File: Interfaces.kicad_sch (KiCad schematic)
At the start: 0 parts

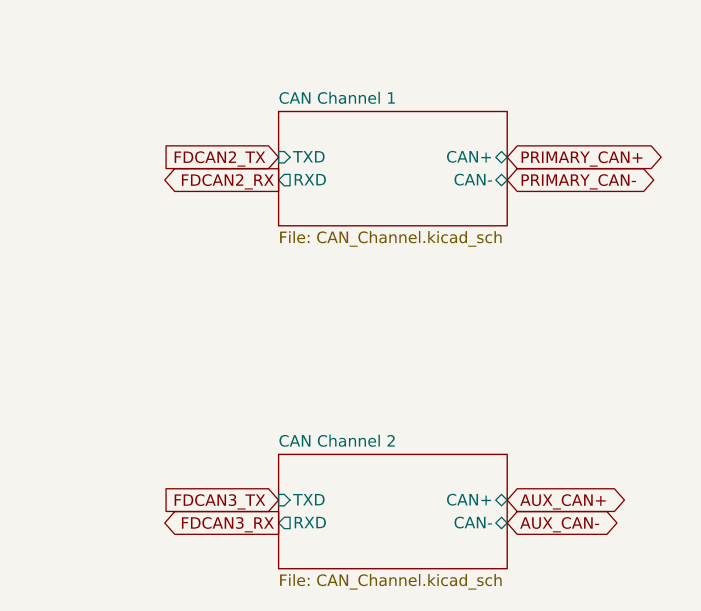
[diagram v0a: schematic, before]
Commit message: add power, some mcu components
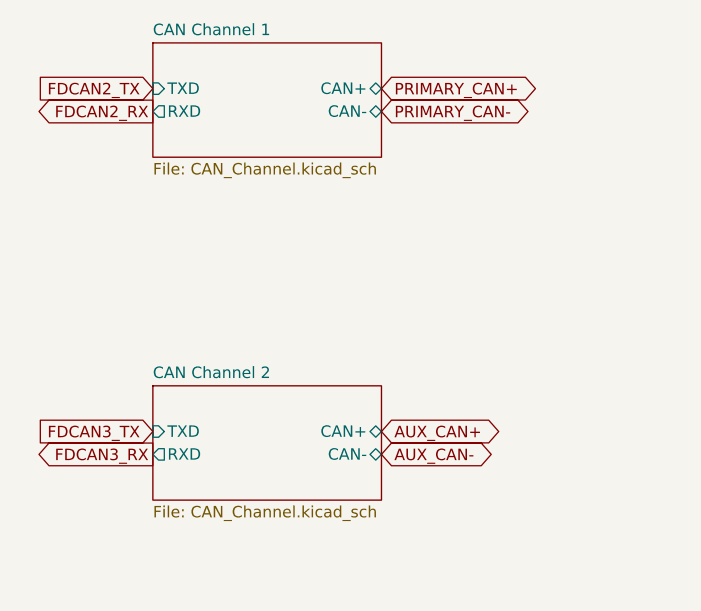
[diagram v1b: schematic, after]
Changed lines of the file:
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@@
 	(global_label "AUX_CAN-"
 		(shape bidirectional)
-		(at 87.63 86.36 0)
+		(at 73.66 78.74 0)
 		(fields_autoplaced yes)
 		(effects
@@
 		)
 		(property "Intersheetrefs" "${INTERSHEET_REFS}"
-			(at 101.5842 86.36 0)
+			(at 87.6142 78.74 0)
 			(effects
 				(font
@@
 	(global_label "FDCAN2_RX"
 		(shape output)
-		(at 62.23 48.26 180)
+		(at 48.26 40.64 180)
 		(fields_autoplaced yes)
 		(effects
@@
 		)
 		(property "Intersheetrefs" "${INTERSHEET_REFS}"
-			(at 48.5405 48.26 0)
+			(at 34.5705 40.64 0)
 			(effects
 				(font
@@
 	(global_label "PRIMARY_CAN+"
 		(shape bidirectional)
-		(at 87.63 45.72 0)
+		(at 73.66 38.1 0)
 		(fields_autoplaced yes)
 		(effects
@@
 		)
 		(property "Intersheetrefs" "${INTERSHEET_REFS}"
-			(at 105.999 45.72 0)
+			(at 92.029 38.1 0)
 			(effects
 				(font
@@
 	(global_label "FDCAN2_TX"
 		(shape input)
-		(at 62.23 45.72 180)
+		(at 48.26 38.1 180)
 		(fields_autoplaced yes)
 		(effects
@@
 		)
 		(property "Intersheetrefs" "${INTERSHEET_REFS}"
-			(at 48.8429 45.72 0)
+			(at 34.8729 38.1 0)
 			(effects
 				(font
@@
 	(global_label "AUX_CAN+"
 		(shape bidirectional)
-		(at 87.63 83.82 0)
+		(at 73.66 76.2 0)
 		(fields_autoplaced yes)
 		(effects
@@
 		)
 		(property "Intersheetrefs" "${INTERSHEET_REFS}"
-			(at 101.5842 83.82 0)
+			(at 87.6142 76.2 0)
 			(effects
 				(font
@@
 	(global_label "PRIMARY_CAN-"
 		(shape bidirectional)
-		(at 87.63 48.26 0)
+		(at 73.66 40.64 0)
 		(fields_autoplaced yes)
 		(effects
@@
 		)
 		(property "Intersheetrefs" "${INTERSHEET_REFS}"
-			(at 105.999 48.26 0)
+			(at 92.029 40.64 0)
 			(effects
 				(font
@@
 	(global_label "FDCAN3_RX"
 		(shape output)
-		(at 62.23 86.36 180)
+		(at 48.26 78.74 180)
 		(fields_autoplaced yes)
 		(effects
@@
 		)
 		(property "Intersheetrefs" "${INTERSHEET_REFS}"
-			(at 48.5405 86.36 0)
+			(at 34.5705 78.74 0)
 			(effects
 				(font
@@
 	(global_label "FDCAN3_TX"
 		(shape input)
-		(at 62.23 83.82 180)
+		(at 48.26 76.2 180)
 		(fields_autoplaced yes)
 		(effects
@@
 		)
 		(property "Intersheetrefs" "${INTERSHEET_REFS}"
-			(at 48.8429 83.82 0)
+			(at 34.8729 76.2 0)
 			(effects
 				(font
@@
 	)
 	(sheet
-		(at 62.23 40.64)
+		(at 48.26 33.02)
 		(size 25.4 12.7)
 		(exclude_from_sim no)
@@
 		)
 		(property "Sheetname" "CAN Channel 1"
-			(at 62.23 39.9284 0)
+			(at 48.26 32.3084 0)
 			(effects
 				(font
@@
 		)
 		(property "Sheetfile" "CAN_Channel.kicad_sch"
-			(at 62.23 53.9246 0)
+			(at 48.26 46.3046 0)
 			(effects
 				(font
@@
 		)
 		(pin "CAN+" bidirectional
-			(at 87.63 45.72 0)
+			(at 73.66 38.1 0)
 			(effects
 				(font
@@
 		)
 		(pin "CAN-" bidirectional
-			(at 87.63 48.26 0)
+			(at 73.66 40.64 0)
 			(effects
 				(font
@@
 		)
 		(pin "TXD" input
-			(at 62.23 45.72 180)
+			(at 48.26 38.1 180)
 			(effects
 				(font
@@
 		)
 		(pin "RXD" output
-			(at 62.23 48.26 180)
+			(at 48.26 40.64 180)
 			(effects
 				(font
@@
 	)
 	(sheet
-		(at 62.23 78.74)
+		(at 48.26 71.12)
 		(size 25.4 12.7)
 		(exclude_from_sim no)
@@
 		)
 		(property "Sheetname" "CAN Channel 2"
-			(at 62.23 78.0284 0)
+			(at 48.26 70.4084 0)
 			(effects
 				(font
@@
 		)
 		(property "Sheetfile" "CAN_Channel.kicad_sch"
-			(at 62.23 92.0246 0)
+			(at 48.26 84.4046 0)
 			(effects
 				(font
@@
 		)
 		(pin "CAN+" bidirectional
-			(at 87.63 83.82 0)
+			(at 73.66 76.2 0)
 			(effects
 				(font
@@
 		)
 		(pin "CAN-" bidirectional
-			(at 87.63 86.36 0)
+			(at 73.66 78.74 0)
 			(effects
 				(font
@@
 		)
 		(pin "TXD" input
-			(at 62.23 83.82 180)
+			(at 48.26 76.2 180)
 			(effects
 				(font
@@
 		)
 		(pin "RXD" output
-			(at 62.23 86.36 180)
-			(effects
-				(font
+			(at 48.26 78.74 180)
+			(effects
+				(font

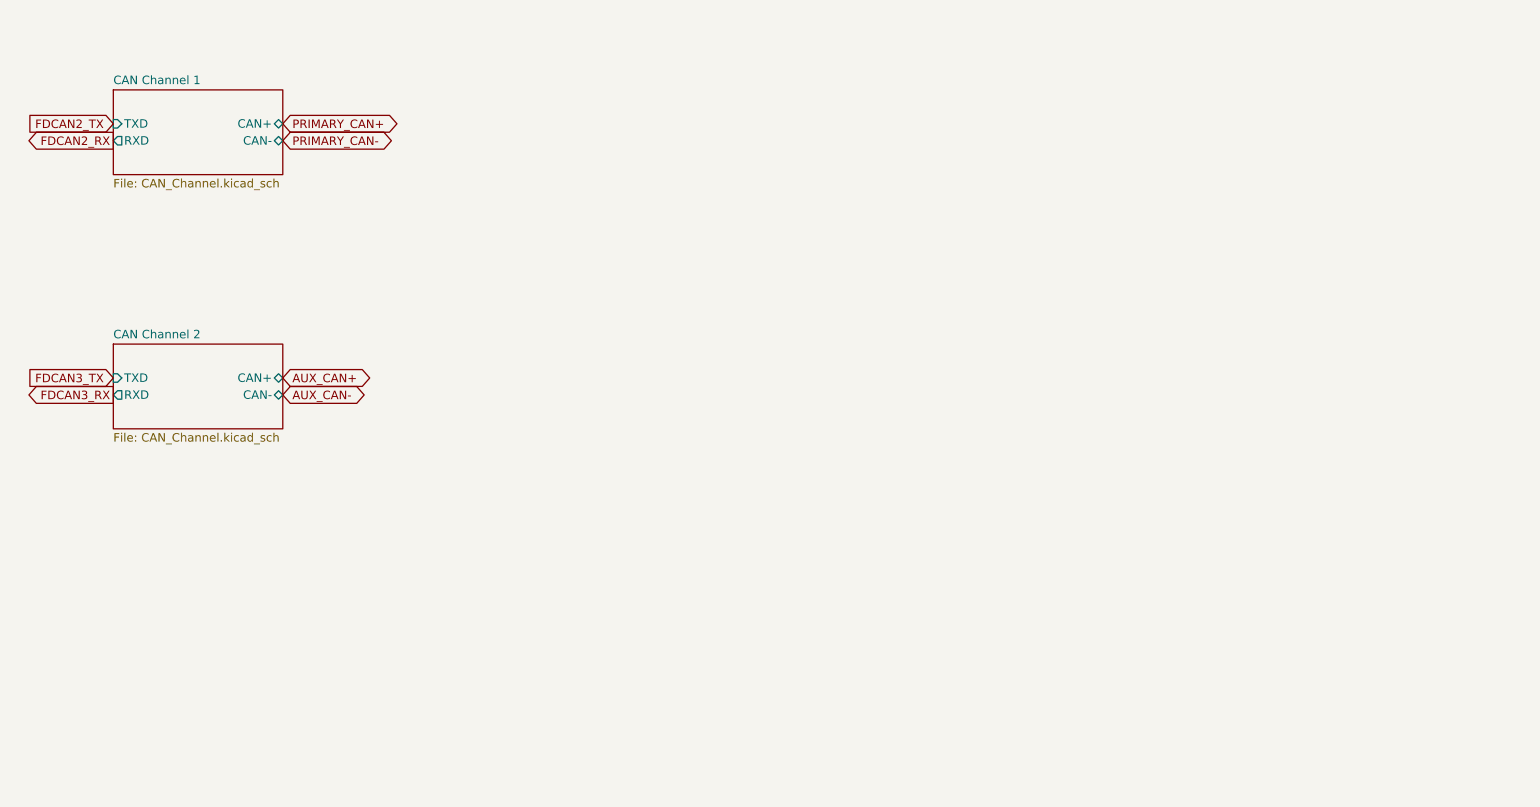
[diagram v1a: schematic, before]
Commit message: complete schematic, initial board layout
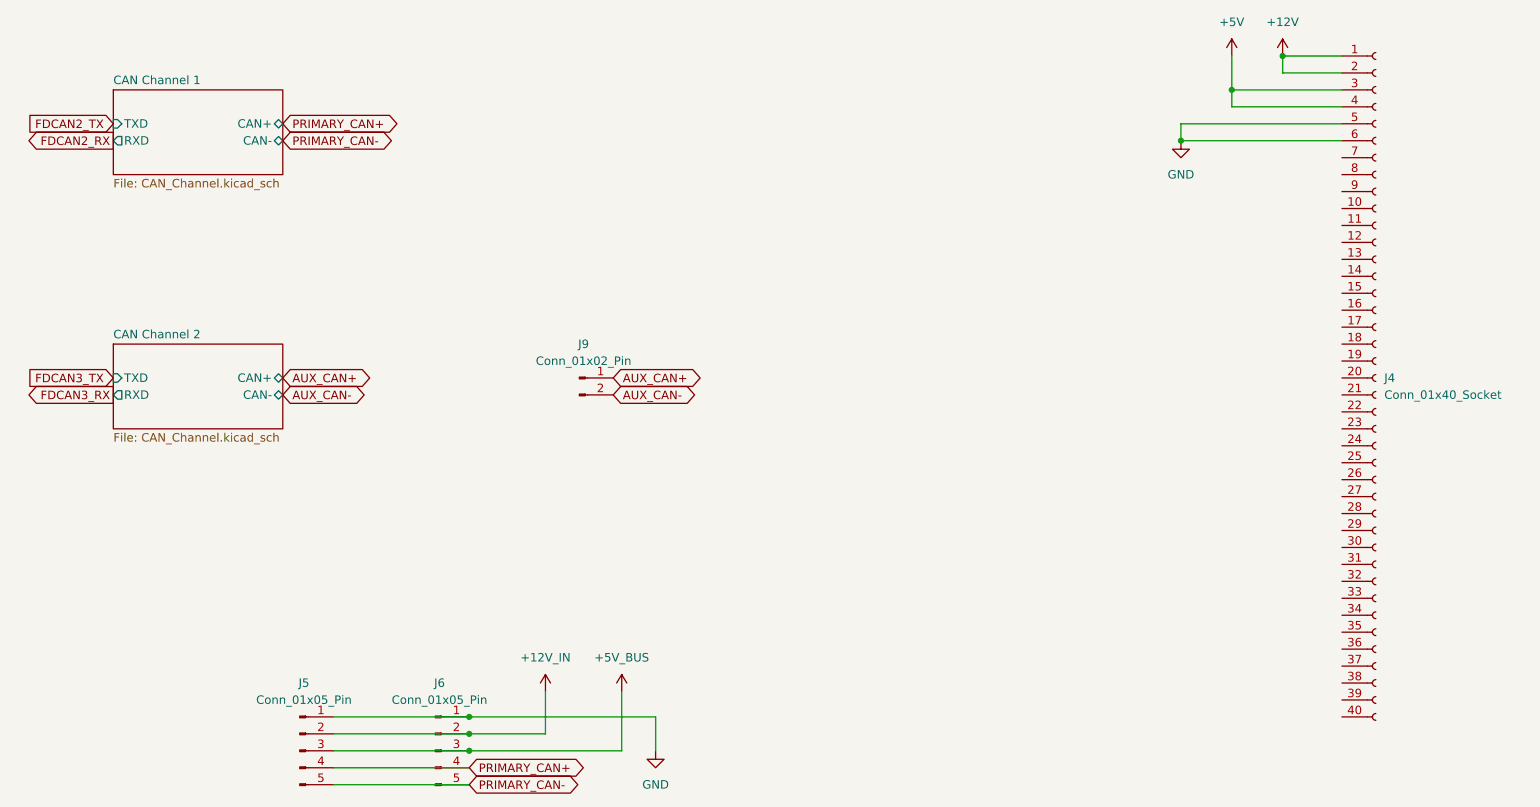
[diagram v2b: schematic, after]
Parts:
- added J4: Conn_01x40_Socket, Connector_PinSocket_2.54mm:PinSocket_1x40_P2.54mm_Horizontal, symbol Connector:Conn_01x40_Socket
- added J5, J6: Conn_01x05_Pin, Connector_Molex:Molex_Micro-Fit_3.0_43650-0515_1x05_P3.00mm_Vertical, symbol Connector:Conn_01x05_Pin
- added J9: Conn_01x02_Pin, Connector_Molex:Molex_Micro-Fit_3.0_43650-0215_1x02_P3.00mm_Vertical, symbol Connector:Conn_01x02_Pin
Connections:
- net AUX_CAN+: now also J9.1 (Pin_1)
- net AUX_CAN-: now also J9.2 (Pin_2)
- net PRIMARY_CAN+: now also J5.4 (Pin_4), J6.4 (Pin_4)
- net PRIMARY_CAN-: now also J5.5 (Pin_5), J6.5 (Pin_5)
- new net +12V: J4.1 (Pin_1), J4.2 (Pin_2)
- new net +12V_IN: J5.2 (Pin_2), J6.2 (Pin_2)
- new net +5V: J4.3 (Pin_3), J4.4 (Pin_4)
- new net +5V_BUS: J5.3 (Pin_3), J6.3 (Pin_3)
- new net GND: J4.5 (Pin_5), J4.6 (Pin_6), J5.1 (Pin_1), J6.1 (Pin_1)

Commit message: completed layout and routing
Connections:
- net GND: now also J4.39 (Pin_39), J4.40 (Pin_40)
- net IO_PC7: now reaches J4.10 (Pin_10)
- net IO_PC8: now reaches J4.11 (Pin_11)
- net IO_PC9: now reaches J4.12 (Pin_12)
- net IO_PA8: now reaches J4.13 (Pin_13)
- net IO_PA9: now reaches J4.14 (Pin_14)
- net IO_PA10: now reaches J4.15 (Pin_15)
- net IO_PB10: now reaches J4.16 (Pin_16)
- net IO_PB2: now reaches J4.17 (Pin_17)
- net IO_PB1: now reaches J4.18 (Pin_18)
- net IO_PC5: now reaches J4.19 (Pin_19)
- net IO_PC4: now reaches J4.20 (Pin_20)
- net IO_PA7: now reaches J4.21 (Pin_21)
- net IO_PA5: now reaches J4.22 (Pin_22)
- net IO_PA3: now reaches J4.23 (Pin_23)
- net IO_PC3: now reaches J4.24 (Pin_24)
- net IO_PC2: now reaches J4.25 (Pin_25)
- net IO_PC1: now reaches J4.26 (Pin_26)
- net IO_PC0: now reaches J4.27 (Pin_27)
- net IO_PC15: now reaches J4.28 (Pin_28)
- net IO_PC14: now reaches J4.29 (Pin_29)
- net IO_PA15: now reaches J4.30 (Pin_30)
- net IO_PC10: now reaches J4.31 (Pin_31)
- net IO_PC11: now reaches J4.32 (Pin_32)
- net IO_PC12: now reaches J4.33 (Pin_33)
- net IO_PD2: now reaches J4.34 (Pin_34)
- net IO_PB4: now reaches J4.35 (Pin_35)
- net IO_PB6: now reaches J4.36 (Pin_36)
- net IO_PB7: now reaches J4.37 (Pin_37)
- net IO_PB9: now reaches J4.38 (Pin_38)
- net IO_PB11: now reaches J4.7 (Pin_7)
- net IO_PB15: now reaches J4.8 (Pin_8)
- net IO_PC6: now reaches J4.9 (Pin_9)
